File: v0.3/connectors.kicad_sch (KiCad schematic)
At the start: 6 parts, among them J1 USB4215-03-A, J2 SWD, J3 BAT, J5 UART

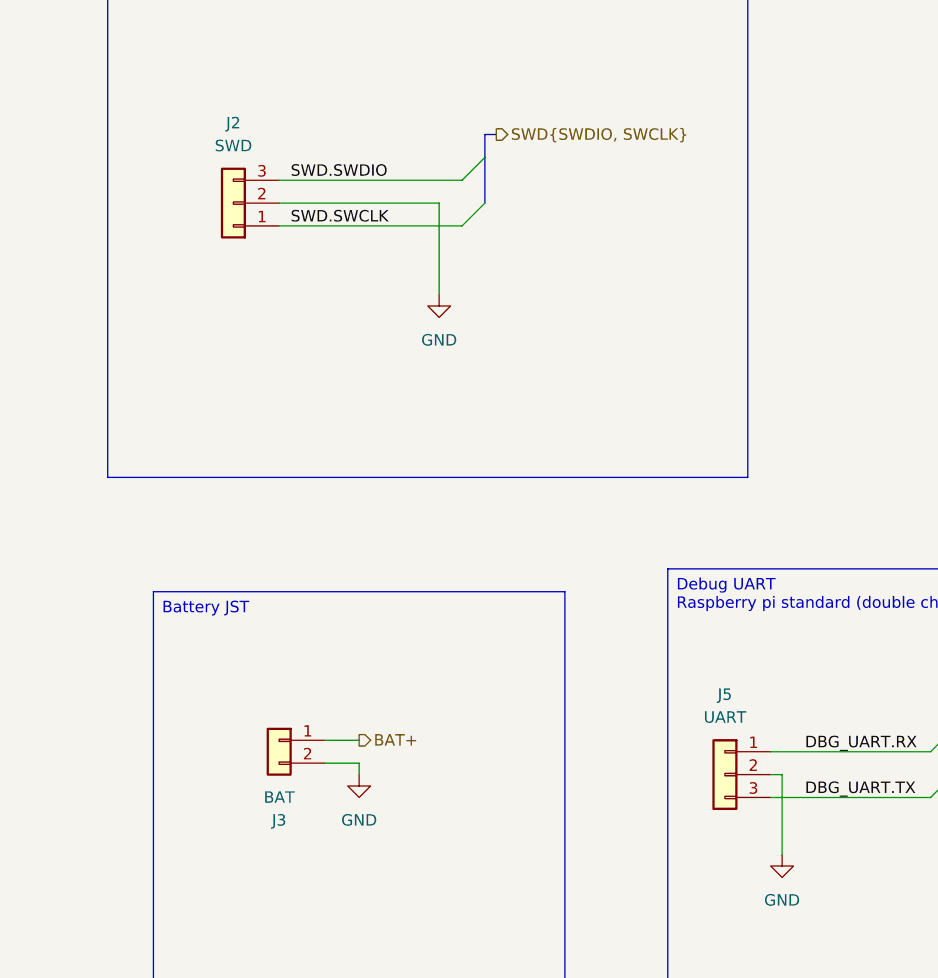
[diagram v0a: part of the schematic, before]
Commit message: v0.3: DRC checks mostly pass, onto final tweaks
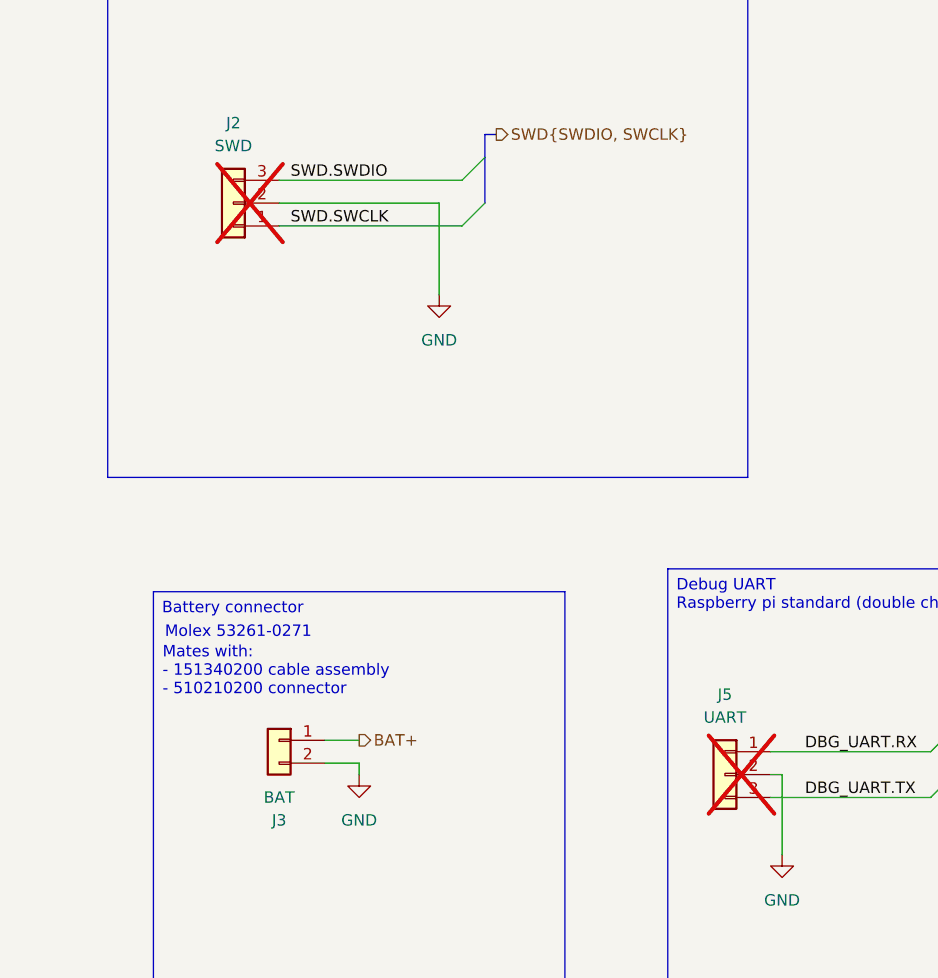
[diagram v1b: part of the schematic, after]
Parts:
- J2, J5: now not fitted
- J3: footprint (none) -> Connector_Molex:Molex_PicoBlade_53261-0271_1x02-1MP_P1.25mm_Horizontal
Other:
- note added: "Mates with: - 151340200 cable assembly - 510210200 connector"
- note added: "Molex 53261-0271"
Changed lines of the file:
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@@
 	(generator_version "9.0")
 	(paper "A4")
+	(text "Mates with:\n- 151340200 cable assembly\n- 510210200 connector"
+		(exclude_from_sim no)
+		(at 159.766 115.57 0)
+		(effects
+			(font
+				(size 1.27 1.27)
+			)
+			(justify left)
+		)
+	)
+	(text "Molex 53261-0271 "
+		(exclude_from_sim no)
+		(at 160.02 111.252 0)
+		(effects
+			(font
+				(size 1.27 1.27)
+			)
+			(justify left)
+		)
+	)
 	(text_box "Debug UART\nRaspberry pi standard (double check)"
 		(exclude_from_sim no)
@@
 		)
 	)
-	(text_box "Battery JST"
+	(text_box "Battery connector"
 		(exclude_from_sim no)
 		(at 158.75 106.68 0)
@@
 		(stroke
 			(width 0)
-			(type default)
+			(type solid)
 		)
 		(fill
@@
 		(in_bom yes)
 		(on_board yes)
-		(dnp no)
+		(dnp yes)
 		(fields_autoplaced yes)
 		(property "Reference" "J5"
@@
 		(in_bom yes)
 		(on_board yes)
-		(dnp no)
+		(dnp yes)
 		(fields_autoplaced yes)
 		(property "Reference" "J2"
@@
 			)
 		)
-		(property "Footprint" ""
+		(property "Footprint" "Connector_Molex:Molex_PicoBlade_53261-0271_1x02-1MP_P1.25mm_Horizontal"
 			(at 172.72 123.19 0)
 			(effects

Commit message: v0.3: update todo a bit
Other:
- note added: "Amphenol 12402012E212A is a drop-in replacement and is a little longer."
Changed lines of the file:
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@@
 	(generator_version "9.0")
 	(paper "A4")
+	(text "Amphenol 12402012E212A is a drop-in replacement and is a little longer."
+		(exclude_from_sim no)
+		(at 97.536 33.528 0)
+		(effects
+			(font
+				(size 1.27 1.27)
+			)
+		)
+	)
 	(text "Mates with:\n- 151340200 cable assembly\n- 510210200 connector"
 		(exclude_from_sim no)
